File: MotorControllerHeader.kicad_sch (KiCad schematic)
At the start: 20 parts, among them J1 Conn_01x02_Pin, J10 Conn_01x02_Socket, J11 Conn_01x02_Pin, J12 Conn_01x02_Socket, J13 Conn_01x02_Pin, J14 Conn_01x02_Socket, J15 Conn_01x02_Pin, J16 Conn_01x02_Socket, J19 Conn_02x04_Odd_Even, J2 Conn_01x02_Socket, J20 Conn_02x04_Odd_Even, J21 Conn_02x04_Odd_Even, J22 Conn_02x04_Odd_Even, J3 Conn_01x02_Pin, J4 Conn_01x02_Socket, J5 Conn_01x02_Pin, J6 Conn_01x02_Socket, J7 Conn_01x02_Pin, J8 Conn_01x02_Socket, J9 Conn_01x02_Pin

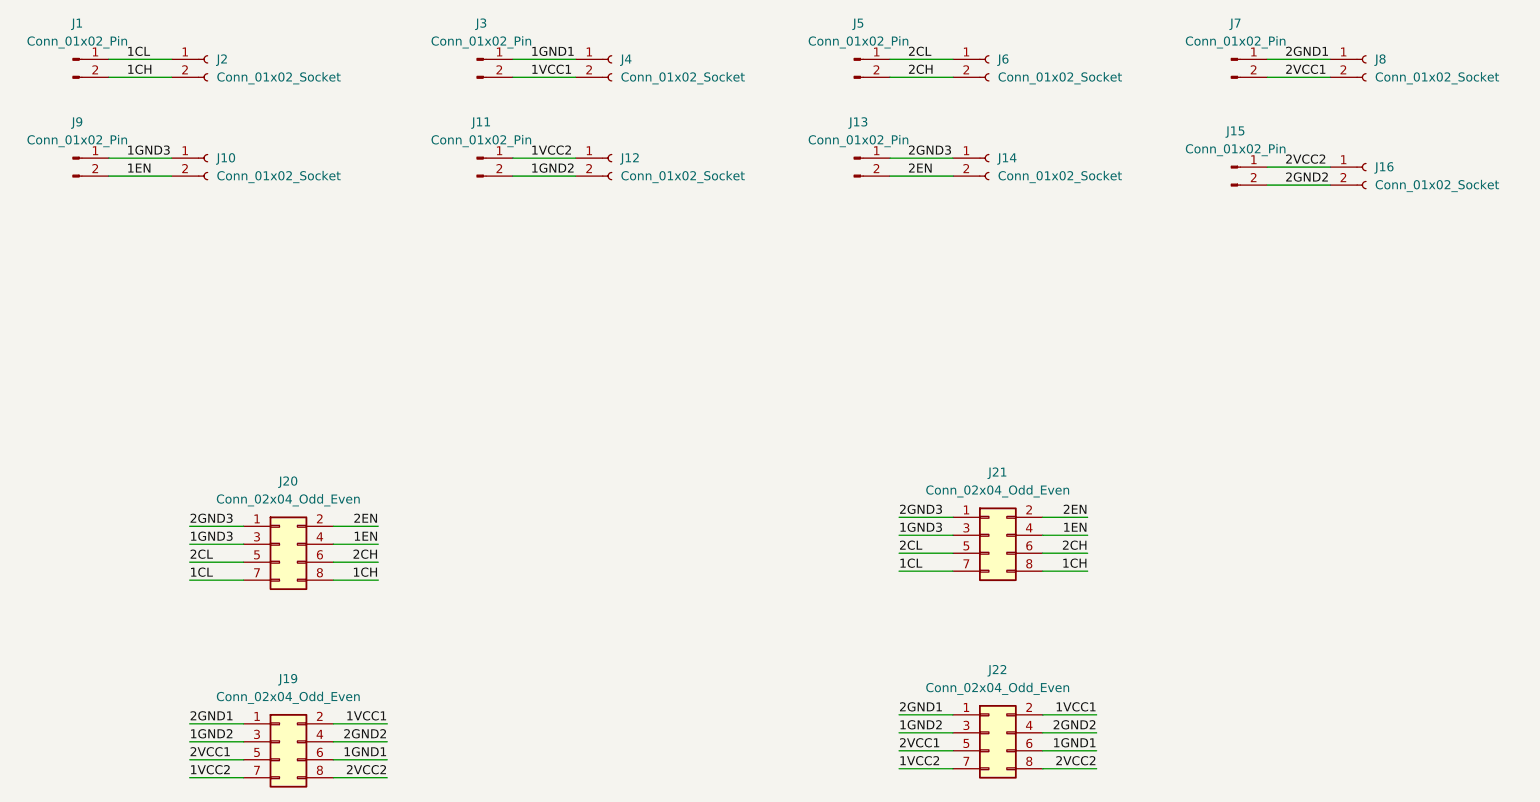
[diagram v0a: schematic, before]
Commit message: Replanned Project: Removed ribbon cable; added female connectors on top and male connectors on bottom
Excludes KiCad backups, autosaves, lock files and .kicad_prl via .gitignore.
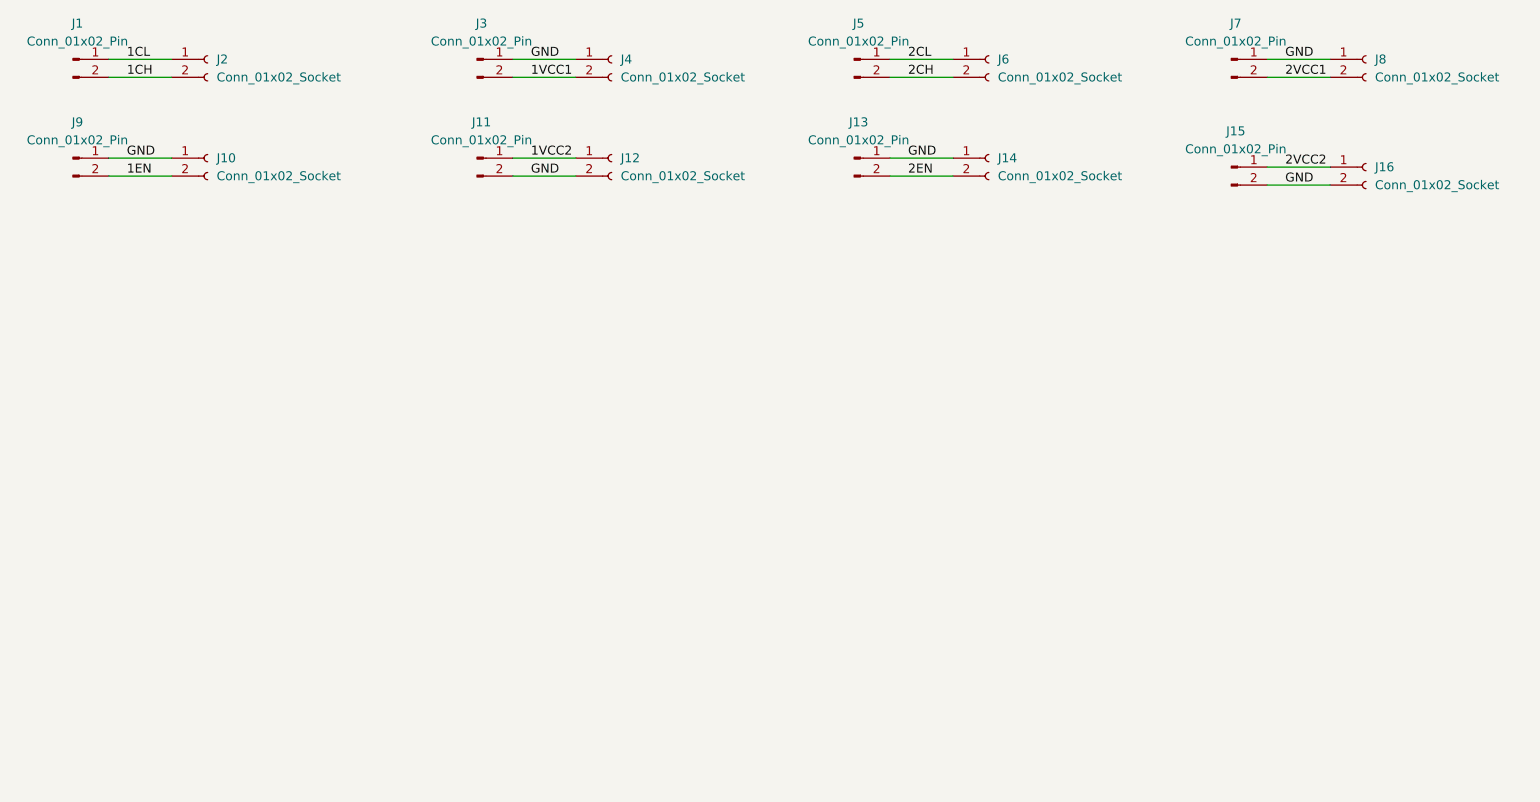
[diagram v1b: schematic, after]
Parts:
- removed J19, J22: Conn_02x04_Odd_Even, Connector_Molex:Molex_Micro-Fit_3.0_43045-0812_2x04_P3.00mm_Vertical, symbol Connector_Generic:Conn_02x04_Odd_Even
- removed J20, J21: Conn_02x04_Odd_Even, Connector_IDC:IDC-Header_2x04_P2.54mm_Vertical, symbol Connector_Generic:Conn_02x04_Odd_Even
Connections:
- net 1GND2 is gone; now on net GND: J11.2 (Pin_2), J12.2 (Pin_2)
- net 1GND3 is gone; now on net GND: J10.1 (Pin_1), J9.1 (Pin_1)
- net 2GND1 is gone; now on net GND: J7.1 (Pin_1), J8.1 (Pin_1)
- net 2GND2 is gone; now on net GND: J15.2 (Pin_2), J16.2 (Pin_2)
- net 2GND3 is gone; now on net GND: J13.1 (Pin_1), J14.1 (Pin_1)
- net 1GND1 renamed GND
